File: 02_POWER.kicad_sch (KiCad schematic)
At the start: 27 parts, among them J201 BATTERY_3PIN, J202 POGO_CHARGE_2PIN, U201 nPM1300-QEXX, U202 TPS63900

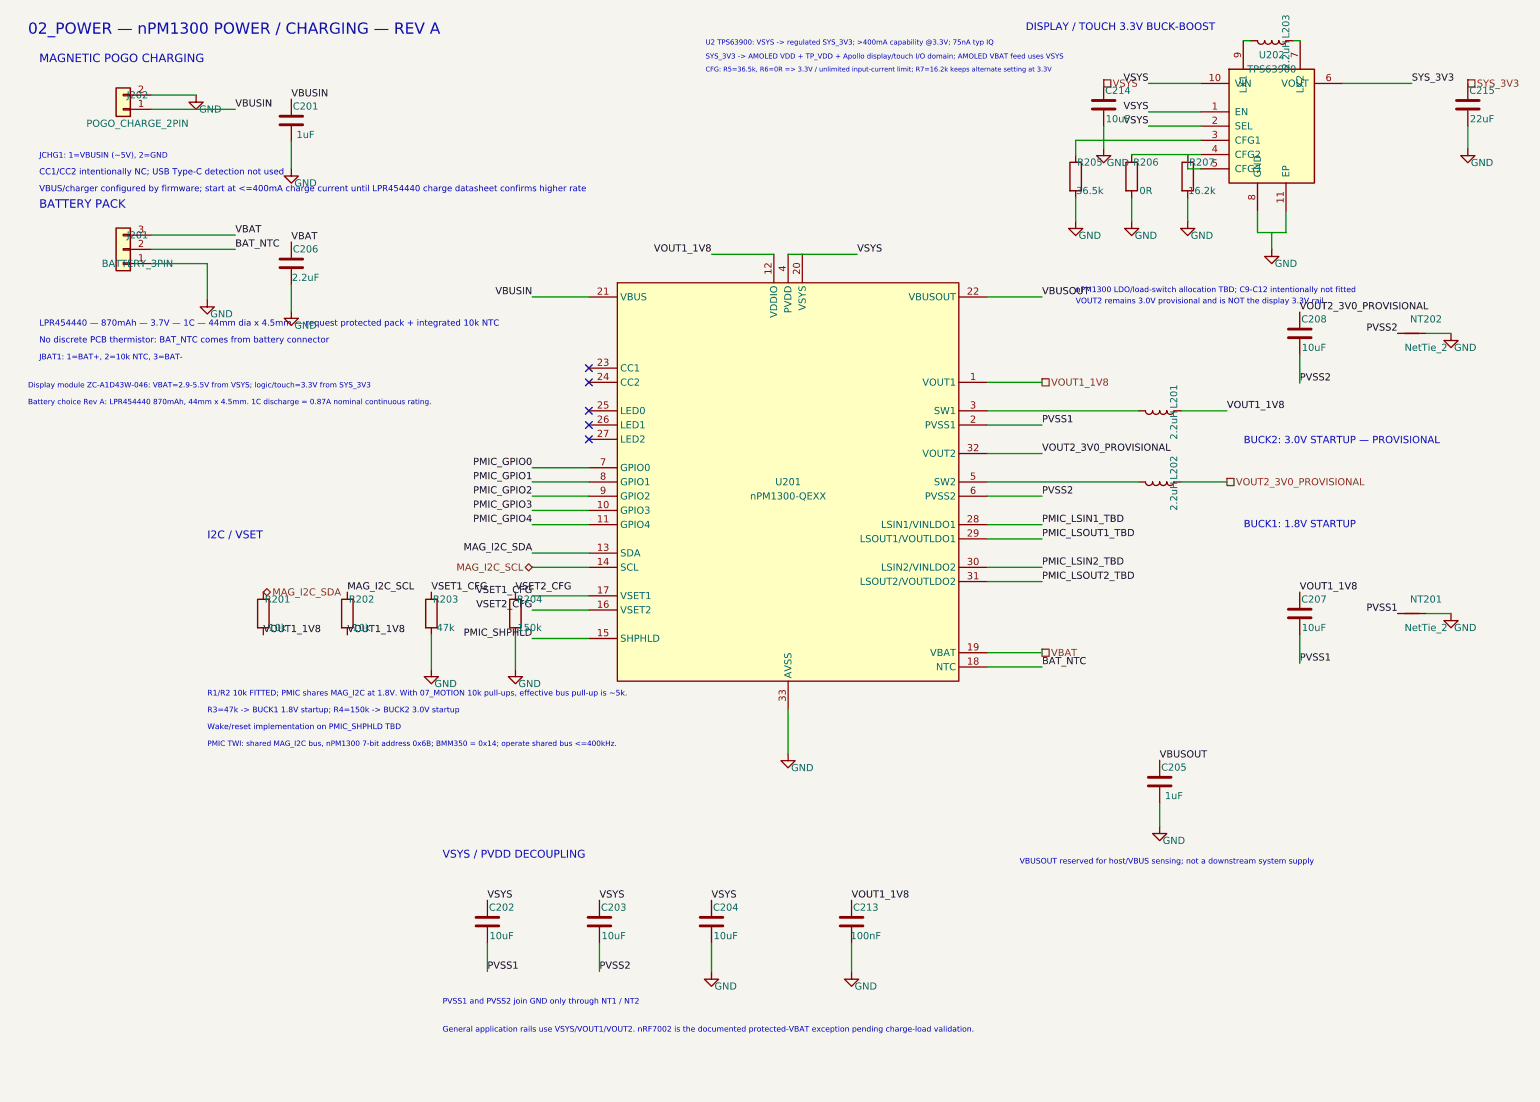
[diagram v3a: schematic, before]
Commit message: fix(kicad): adjudicate and resolve native ERC errors
- Connect SFH7018A D401.7 and D402.7 green cathode pins to green LED drive
  nets per OSRAM pinout (Class A circuit fix)
- Add deliberate no_connect markers to unused pins U11.5 (QOD) and PMIC U201.15
  (SHPHLD), U201.28 (LSIN1), U201.30 (LSIN2) per datasheets (Class B)
- Place PWR_FLAG markers at external power sources: VBUSIN at J202, VBAT and
  GND at J201 (Class C)
- Place PWR_FLAG markers for net ties and post-inductor domains: PVSS1/PVSS2
  at NT201/NT202, PD_GND at NT401/NT402, and WIFI_VDD_BUCK at L601 (Class D)
- Correct symbol pin electrical types: nRF7002 PAVDD<0>/<1> to passive, PCA9306
  VREF2 to passive, and TC2030-CTX-NL nRESET to passive (Class E)
- Retain U12.A1/U13.A1 PPG_VLED undriven error as intentional TBD (Class G)
- Verification: 83/83 hierarchy interfaces match; ERC errors reduced from 18 to 1
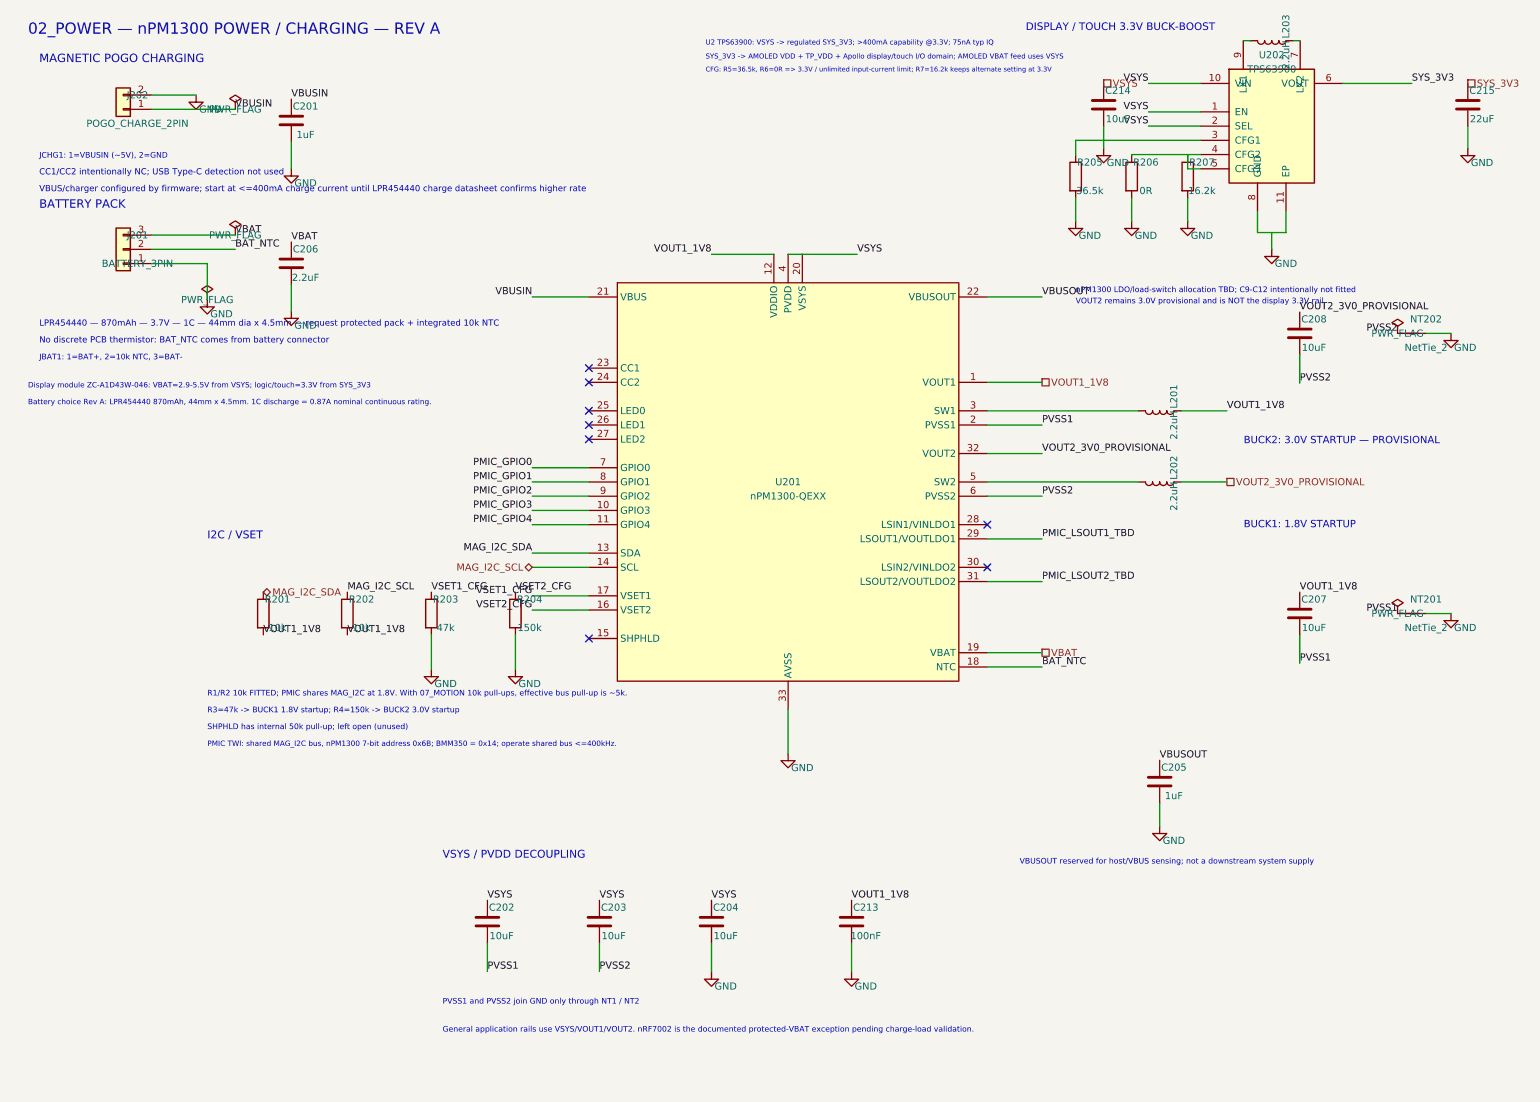
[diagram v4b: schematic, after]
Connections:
- net PMIC_LSIN1_TBD: no longer names the net of U201.28 (LSIN1/VINLDO1)
- net PMIC_LSIN2_TBD: no longer names the net of U201.30 (LSIN2/VINLDO2)
- net PMIC_SHPHLD: no longer names the net of U201.15 (SHPHLD)
- no-connect marks 5 -> 8
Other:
- note added: "SHPHLD has internal 50k pull-up; left open (unused)"
- note removed: "Wake/reset implementation on PMIC_SHPHLD TBD"

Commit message: feat(kicad): assign and audit Rev-A footprints
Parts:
- C201, C205, C206, C213: footprint (none) -> Capacitor_SMD:C_0402_1005Metric
- C202, C203, C204, C207, C208: footprint (none) -> Capacitor_SMD:C_0603_1608Metric
- J201: footprint (none) -> sportwatch_custom:BatteryPad_3Pin_SMD
- J202: footprint (none) -> sportwatch_custom:PogoPad_2Pin_SMD
- L201, L202: footprint (none) -> Inductor_SMD:L_0603_1608Metric
- L203: footprint (none) -> sportwatch_custom:L_2016_2016Metric
- NT201, NT202: footprint (none) -> NetTie:NetTie-2_SMD_Pad0.5mm
- R201, R202, R203, R204: footprint (none) -> Resistor_SMD:R_0402_1005Metric
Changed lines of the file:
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@@
 			)
 		)
-		(property "Footprint" ""
+		(property "Footprint" "Capacitor_SMD:C_0603_1608Metric"
 			(at 120 175 0)
 			(hide yes)
@@
 			)
 		)
-		(property "Footprint" ""
+		(property "Footprint" "NetTie:NetTie-2_SMD_Pad0.5mm"
 			(at 265 120 0)
 			(hide yes)
@@
 			)
 		)
-		(property "Footprint" ""
+		(property "Footprint" "Capacitor_SMD:C_0603_1608Metric"
 			(at 245 70 0)
 			(hide yes)
@@
 			)
 		)
-		(property "Footprint" ""
+		(property "Footprint" "sportwatch_custom:L_2016_2016Metric"
 			(at 240 17.76 0)
 			(hide yes)
@@
 			)
 		)
-		(property "Footprint" ""
+		(property "Footprint" "sportwatch_custom:PogoPad_2Pin_SMD"
 			(at 35 30 0)
 			(hide yes)
@@
 			)
 		)
-		(property "Footprint" ""
+		(property "Footprint" "Capacitor_SMD:C_0402_1005Metric"
 			(at 220 150 0)
 			(hide yes)
@@
 			)
 		)
-		(property "Footprint" ""
+		(property "Footprint" "Capacitor_SMD:C_0603_1608Metric"
 			(at 100 175 0)
 			(hide yes)
@@
 			)
 		)
-		(property "Footprint" ""
+		(property "Footprint" "NetTie:NetTie-2_SMD_Pad0.5mm"
 			(at 265 70 0)
 			(hide yes)
@@
 			)
 		)
-		(property "Footprint" ""
+		(property "Footprint" "Capacitor_SMD:C_0402_1005Metric"
 			(at 165 175 0)
 			(hide yes)
@@
 			)
 		)
-		(property "Footprint" ""
+		(property "Footprint" "Resistor_SMD:R_0402_1005Metric"
 			(at 90 120 0)
 			(hide yes)
@@
 			)
 		)
-		(property "Footprint" ""
+		(property "Footprint" "sportwatch_custom:BatteryPad_3Pin_SMD"
 			(at 35 55 0)
 			(hide yes)
@@
 			)
 		)
-		(property "Footprint" ""
+		(property "Footprint" "Inductor_SMD:L_0603_1608Metric"
 			(at 220 83.82 0)
 			(hide yes)
@@
 			)
 		)
-		(property "Footprint" ""
+		(property "Footprint" "Inductor_SMD:L_0603_1608Metric"
 			(at 220 96.52 0)
 			(hide yes)
@@
 			)
 		)
-		(property "Footprint" ""
+		(property "Footprint" "Resistor_SMD:R_0402_1005Metric"
 			(at 105 120 0)
 			(hide yes)
@@
 			)
 		)
-		(property "Footprint" ""
+		(property "Footprint" "Capacitor_SMD:C_0402_1005Metric"
 			(at 65 32 0)
 			(hide yes)
@@
 			)
 		)
-		(property "Footprint" ""
+		(property "Footprint" "Resistor_SMD:R_0402_1005Metric"
 			(at 60 120 0)
 			(hide yes)
@@
 			)
 		)
-		(property "Footprint" ""
+		(property "Footprint" "Capacitor_SMD:C_0402_1005Metric"
 			(at 65 57.5 0)
 			(hide yes)
@@
 			)
 		)
-		(property "Footprint" ""
+		(property "Footprint" "Capacitor_SMD:C_0603_1608Metric"
 			(at 245 120 0)
 			(hide yes)
@@
 			)
 		)
-		(property "Footprint" ""
+		(property "Footprint" "Resistor_SMD:R_0402_1005Metric"
 			(at 75 120 0)
 			(hide yes)
@@
 			)
 		)
-		(property "Footprint" ""
+		(property "Footprint" "Capacitor_SMD:C_0603_1608Metric"
 			(at 140 175 0)
 			(hide yes)

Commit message: fix(pcba): resolve post-footprint freeze sanity items and freeze footprints
- Resolve Flatpak KICAD10_SYMBOL_DIR path discrepancy, reducing lib_symbol_issues to 0
- Re-audit Y1 and Y102 crystals against NDK NX1612SA; ground pads 2/4 for RF shield
- Reclassify SW1..SW5, J201, and J202 as Class C pending mechanical enclosure freeze
- Verify native ERC (0 errors), 83 interfaces (checked=83 mismatches=0), and 0 unintended net changes
- Add docs/project/post_footprint_freeze_sanity.md with FOOTPRINT FREEZE: PASS
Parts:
- J201: footprint sportwatch_custom:BatteryPad_3Pin_SMD -> (none)
- J202: footprint sportwatch_custom:PogoPad_2Pin_SMD -> (none)
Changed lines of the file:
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@@
 			)
 		)
-		(property "Footprint" "sportwatch_custom:PogoPad_2Pin_SMD"
+		(property "Footprint" ""
 			(at 35 30 0)
 			(hide yes)
@@
 			)
 		)
-		(property "Footprint" "sportwatch_custom:BatteryPad_3Pin_SMD"
+		(property "Footprint" ""
 			(at 35 55 0)
 			(hide yes)

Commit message: foundation correction
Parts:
- removed J202: POGO_CHARGE_2PIN, symbol Connector_Generic:Conn_01x02
- C201, C202, C203, C204, C205, C206, C207, C208, C213, C214, C215, J201, L201, L202, L203, NT201, NT202, R201, R202, R203, R204, R205, R206, R207, U201, U202: Board (none) -> MAIN
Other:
- note added: "C206 = 2.2uF from VBAT to GND. Battery functional conductors: BAT+ / NTC / BAT-."
- note added: "Charger harness/protection owned by 12_CHARGING; C201 stays local to U201 VBUS"
- note added: "J201 LIVE: 1=GND/BAT-, 2=BAT_NTC, 3=VBAT/BAT+; footprint/MPN TBD"
- note removed: "JBAT1: 1=BAT+, 2=10k NTC, 3=BAT-"
- note removed: "JCHG1: 1=VBUSIN (~5V), 2=GND"
